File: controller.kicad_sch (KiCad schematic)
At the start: 30 parts, among them J501 SWD, J502 USB_C_Receptacle_USB2.0_16P, J503 CAN, SW501 CL-SB_22A-12T, U501 IP4234CZ6, U502 ULN2803A, U503 STM32G431CBTx, U504 MCP2542FDxMF

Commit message: Add some missing footprints and rearranged schematics a bit
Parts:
- C502, C506, C507, C508, C509, C510, C511: footprint (none) -> Capacitor_SMD:C_0603_1608Metric
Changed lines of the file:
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@@
 			)
 		)
-		(property "Footprint" ""
+		(property "Footprint" "Capacitor_SMD:C_0603_1608Metric"
 			(at 53.34 60.96 0)
 			(effects
@@
 			)
 		)
-		(property "Footprint" ""
+		(property "Footprint" "Capacitor_SMD:C_0603_1608Metric"
 			(at 48.26 171.45 0)
 			(effects
@@
 			)
 		)
-		(property "Footprint" ""
+		(property "Footprint" "Capacitor_SMD:C_0603_1608Metric"
 			(at 153.67 173.99 0)
 			(effects
@@
 			)
 		)
-		(property "Footprint" ""
+		(property "Footprint" "Capacitor_SMD:C_0603_1608Metric"
 			(at 59.69 171.45 0)
 			(effects
@@
 			)
 		)
-		(property "Footprint" ""
+		(property "Footprint" "Capacitor_SMD:C_0603_1608Metric"
 			(at 36.83 171.45 0)
 			(effects
@@
 			)
 		)
-		(property "Footprint" ""
+		(property "Footprint" "Capacitor_SMD:C_0603_1608Metric"
 			(at 25.4 171.45 0)
 			(effects
@@
 			)
 		)
-		(property "Footprint" ""
+		(property "Footprint" "Capacitor_SMD:C_0603_1608Metric"
 			(at 165.1 173.99 0)
 			(effects

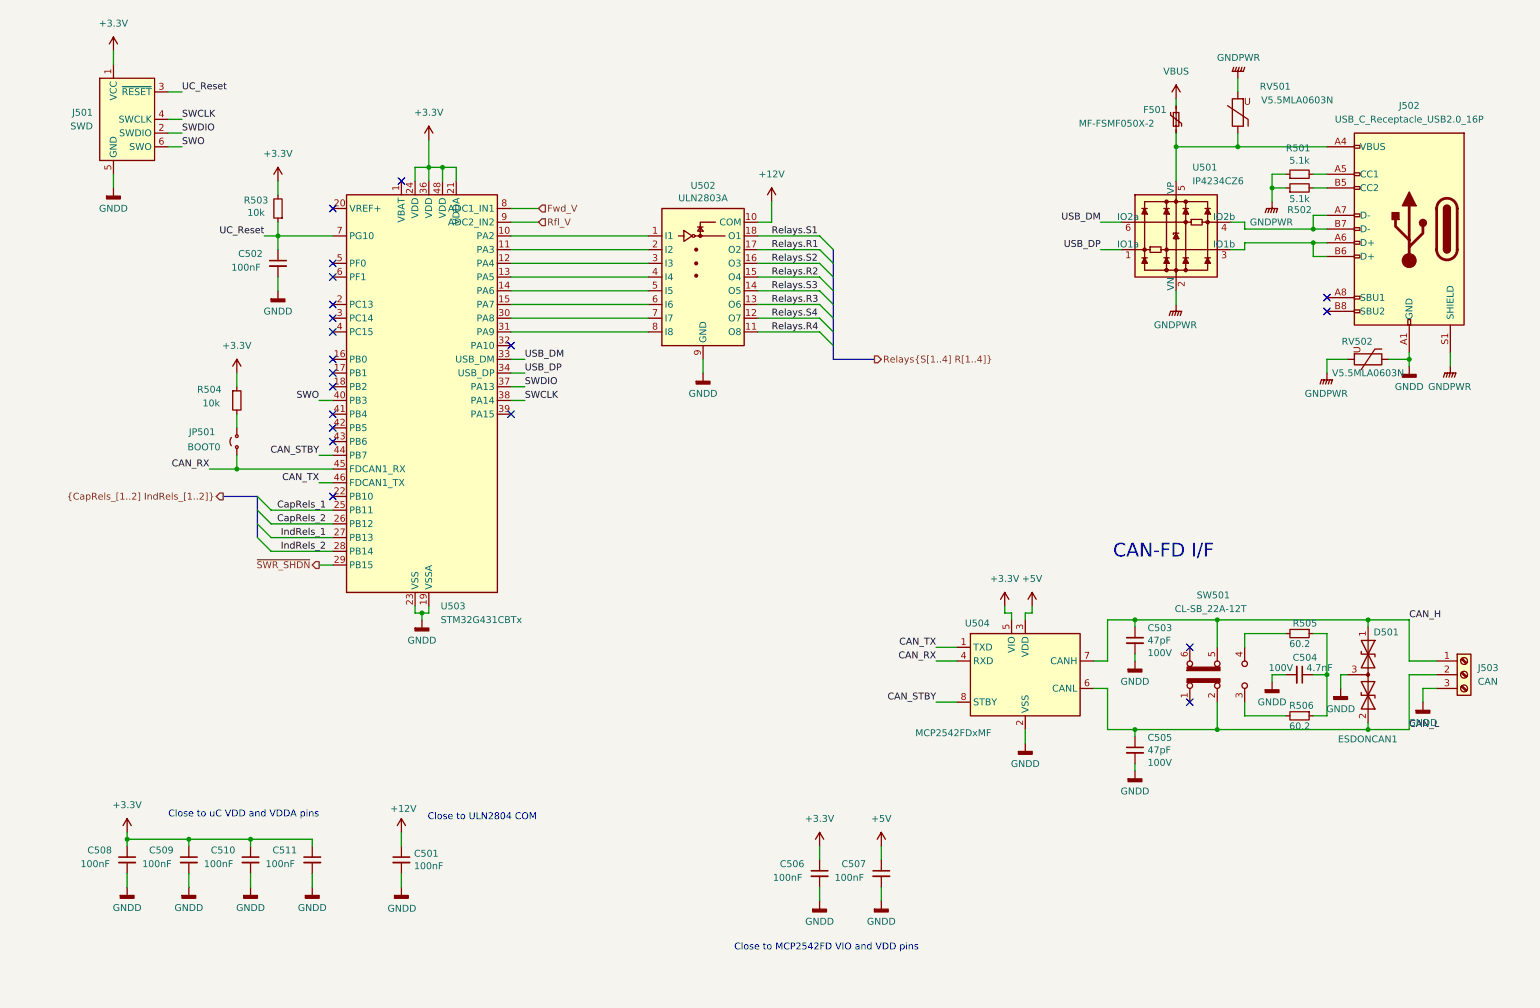
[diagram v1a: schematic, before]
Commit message: Added connectors to top schematic. Added xtal and optocouplers to controller.
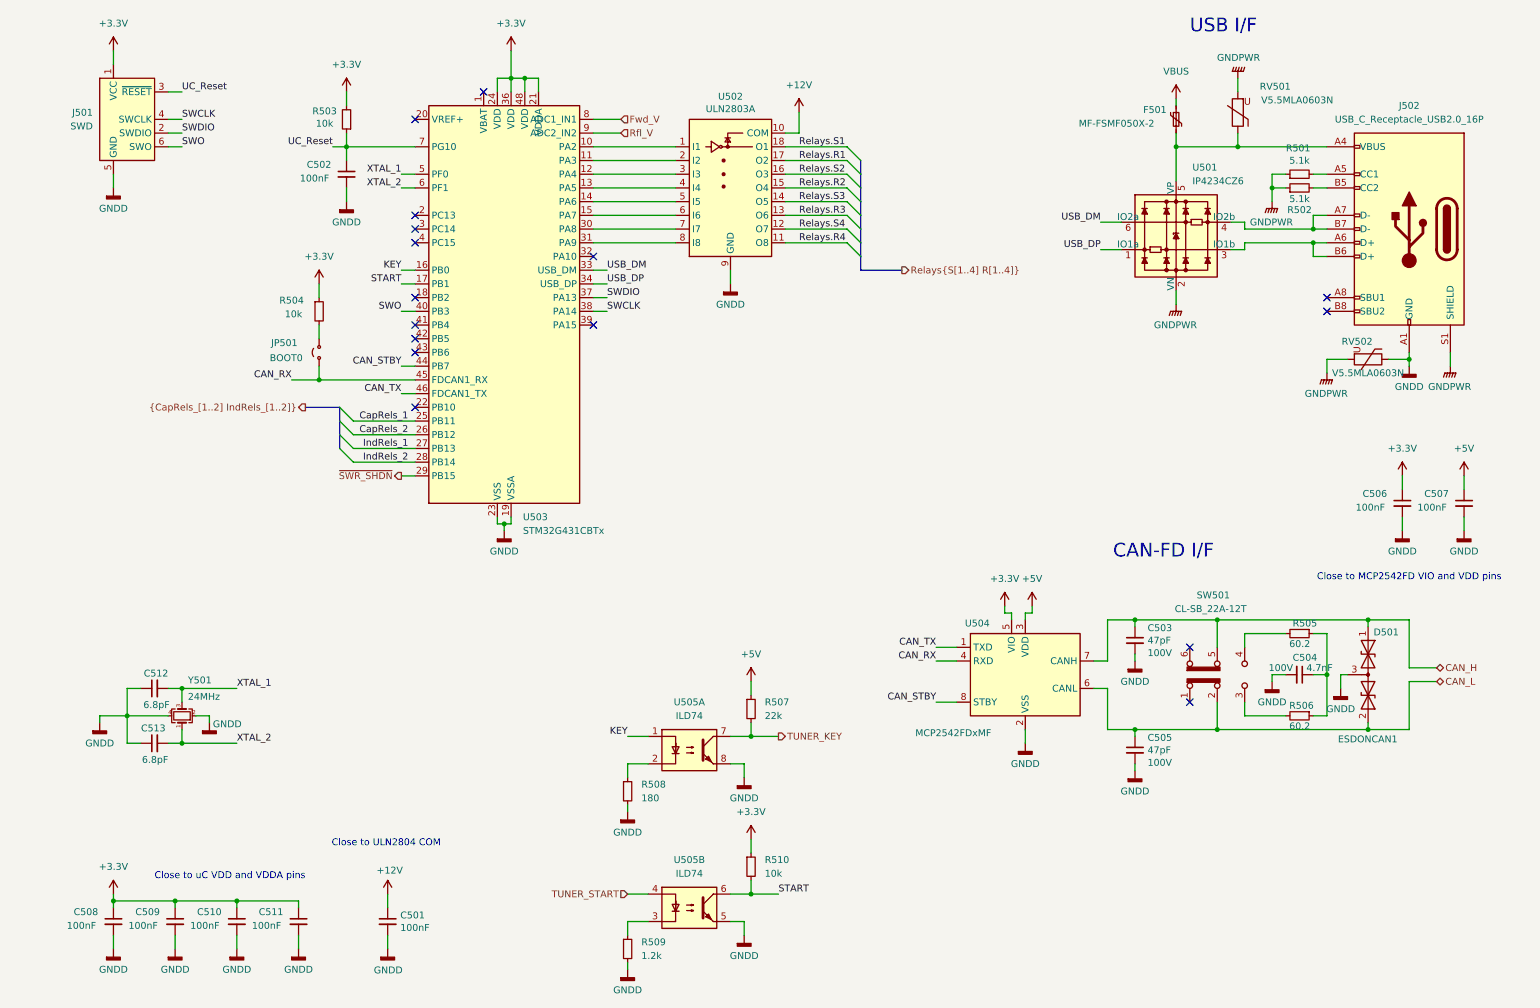
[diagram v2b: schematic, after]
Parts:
- removed J503: CAN, TerminalBlock_4Ucon:TerminalBlock_4Ucon_1x03_P3.50mm_Horizontal, symbol Connector:Screw_Terminal_01x03
- added C512, C513: 6.8pF, Capacitor_SMD:C_0603_1608Metric, symbol Device:C_Small
- added R507: 22k, Resistor_SMD:R_0603_1608Metric, symbol Device:R_Small
- added R508: 180, Resistor_SMD:R_0603_1608Metric, symbol Device:R_Small
- added R509: 1.2k, Resistor_SMD:R_0603_1608Metric, symbol Device:R_Small
- added R510: 10k, Resistor_SMD:R_0603_1608Metric, symbol Device:R_Small
- added U505: ILD74, Package_SO:SOP-8_3.9x4.9mm_P1.27mm, symbol Isolator:ILD74
- added Y501: 24MHz, Crystal:Crystal_SMD_3225-4Pin_3.2x2.5mm, symbol Device:Crystal_GND24_Small
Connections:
- net +3.3V: now also R510.1
- net +5V: now also R507.1
- net GNDD: now also C512.1, C513.1, R508.2, R509.2, U505.5, U505.8, Y501.2, Y501.4
- net KEY: now reaches U503.16 (PB0)
- net KEY: now also U505.1
- net START: now reaches U503.17 (PB1)
- net START: now also R510.2, U505.6
- net XTAL_1: now reaches U503.5 (PF0)
- net XTAL_1: now also C512.2, Y501.3
- net XTAL_2: now reaches U503.6 (PF1)
- net XTAL_2: now also C513.2, Y501.1
- new net: R508.1, U505.2
- new net: R509.1, U505.3
- new net TUNER_KEY: R507.2, U505.7
- new net TUNER_START: U505.4
- no-connect marks 20 -> 16
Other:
- note added: "USB I/F"
- moved on the sheet: C501, C502, C506, C507, C508, C509, C510, C511, JP501, R503, R504, U502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

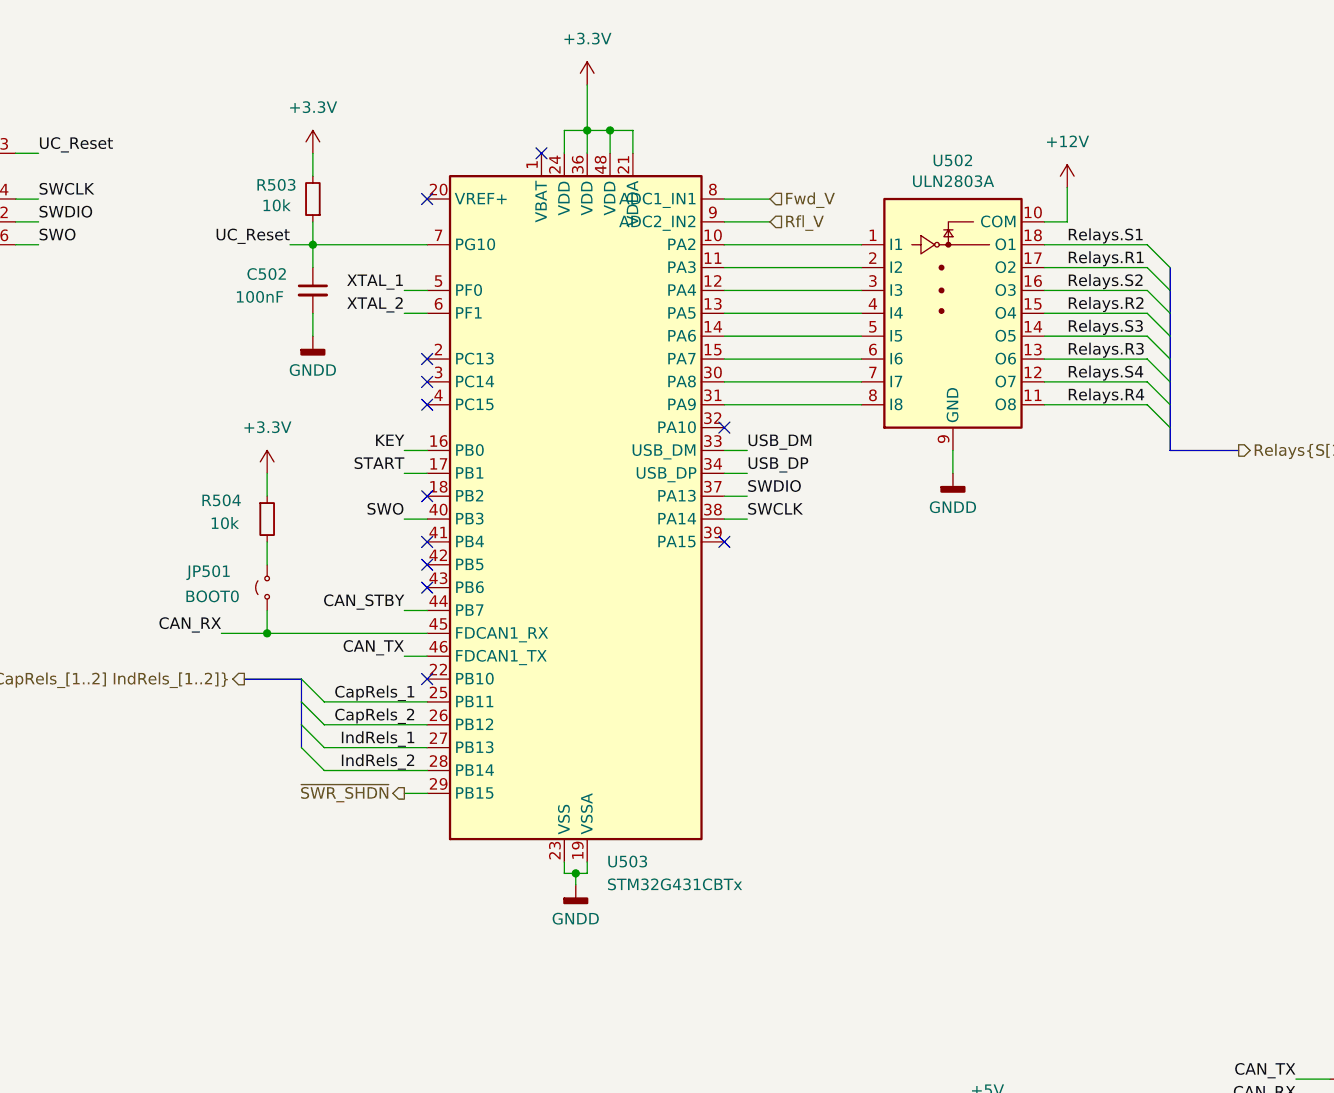
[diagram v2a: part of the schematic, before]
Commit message: Added 'Power', 'Op' and 'Error' LEDs
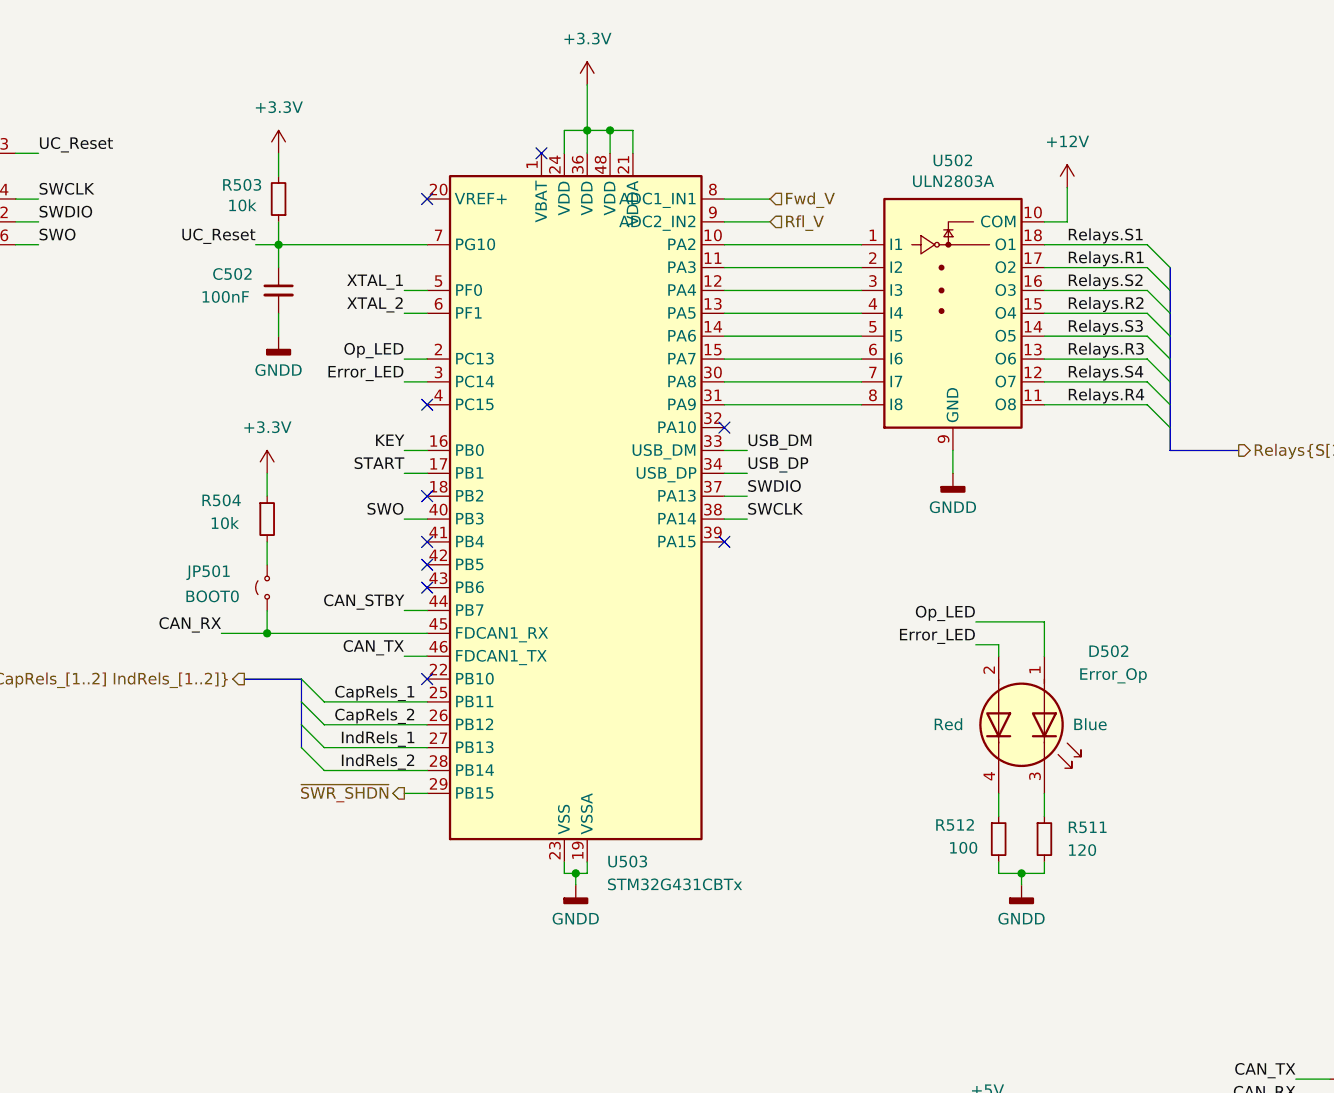
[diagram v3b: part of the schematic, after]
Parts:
- added D502: Error_Op, ZFTuner_Lib:LED_Dual_1615_1.6mm_1.5mm, symbol Device:LED_Dual_AAKK
- added R511: 120, Resistor_SMD:R_0603_1608Metric, symbol Device:R_Small
- added R512: 100, Resistor_SMD:R_0603_1608Metric, symbol Device:R_Small
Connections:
- net GNDD: now also R511.2, R512.2
- net Op_LED: now reaches U503.2 (PC13)
- net Op_LED: now also D502.1 (A1)
- net Error_LED: now reaches U503.3 (PC14)
- net Error_LED: now also D502.2 (A2)
- new net: D502.4 (K2), R512.1
- new net: D502.3 (K1), R511.1
- no-connect marks 16 -> 14
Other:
- moved on the sheet: C502, R503

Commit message: Created PDF of schematic
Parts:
- renumbered C502 to C201, C506 to C202, C507 to C203, C503 to C204, C504 to C205, C512 to C206, C513 to C207, C505 to C208, C508 to C209, C509 to C210, C510 to C211, C511 to C212, C501 to C213, D502 to D201, D501 to D202, F501 to F201, J501 to J201, J502 to J202, JP501 to JP201, R503 to R201, R501 to R202, R502 to R203, R504 to R204, R512 to R205, R511 to R206, R505 to R207, R507 to R208, R506 to R209, R508 to R210, R510 to R211, R509 to R212, RV501 to RV201, RV502 to RV202, SW501 to SW201, U502 to U201, U501 to U202, U503 to U203, U504 to U204, U505 to U205, Y501 to Y201

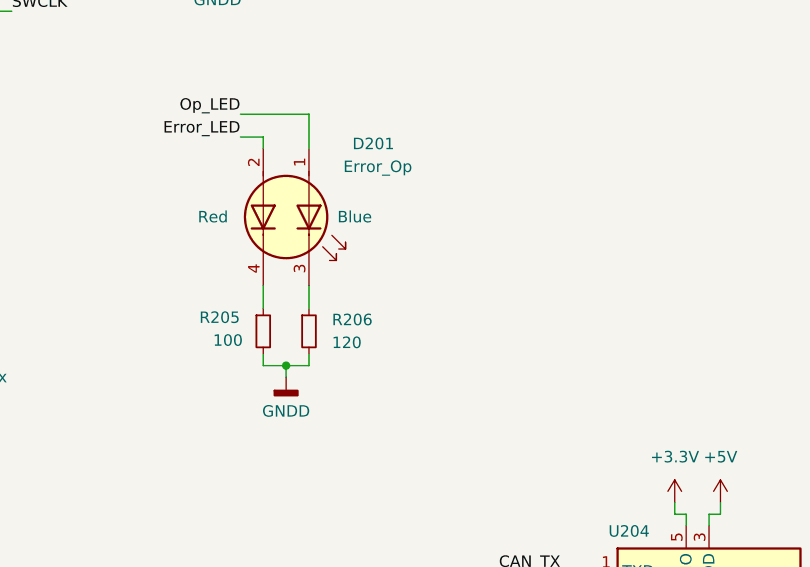
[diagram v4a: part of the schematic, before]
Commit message: Added LEDs part numbers
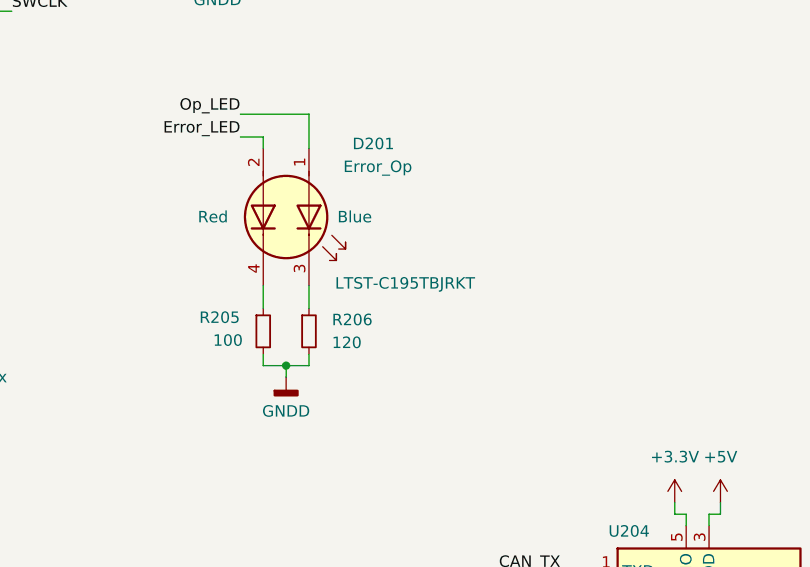
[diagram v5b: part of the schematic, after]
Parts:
- D201: Part (none) -> LTST-C195TBJRKT
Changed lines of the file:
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@@
+			)
+		)
+		(property "Part" "LTST-C195TBJRKT"
+			(at 157.988 100.076 90)
+			(effects
+				(font
+					(size 1.27 1.27)
+				)
 			)
 		)
